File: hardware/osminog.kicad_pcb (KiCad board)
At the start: 2 copper layers, 16 parts, among them IC1 ATTINY2313-S, P1 USB_OTG, P2 CONN_01X02, P3 CONN_02X03, P4 CONN_01X03, P5 CONN_01X03, Q1 BSS138, U1 CH340G, Y1 12

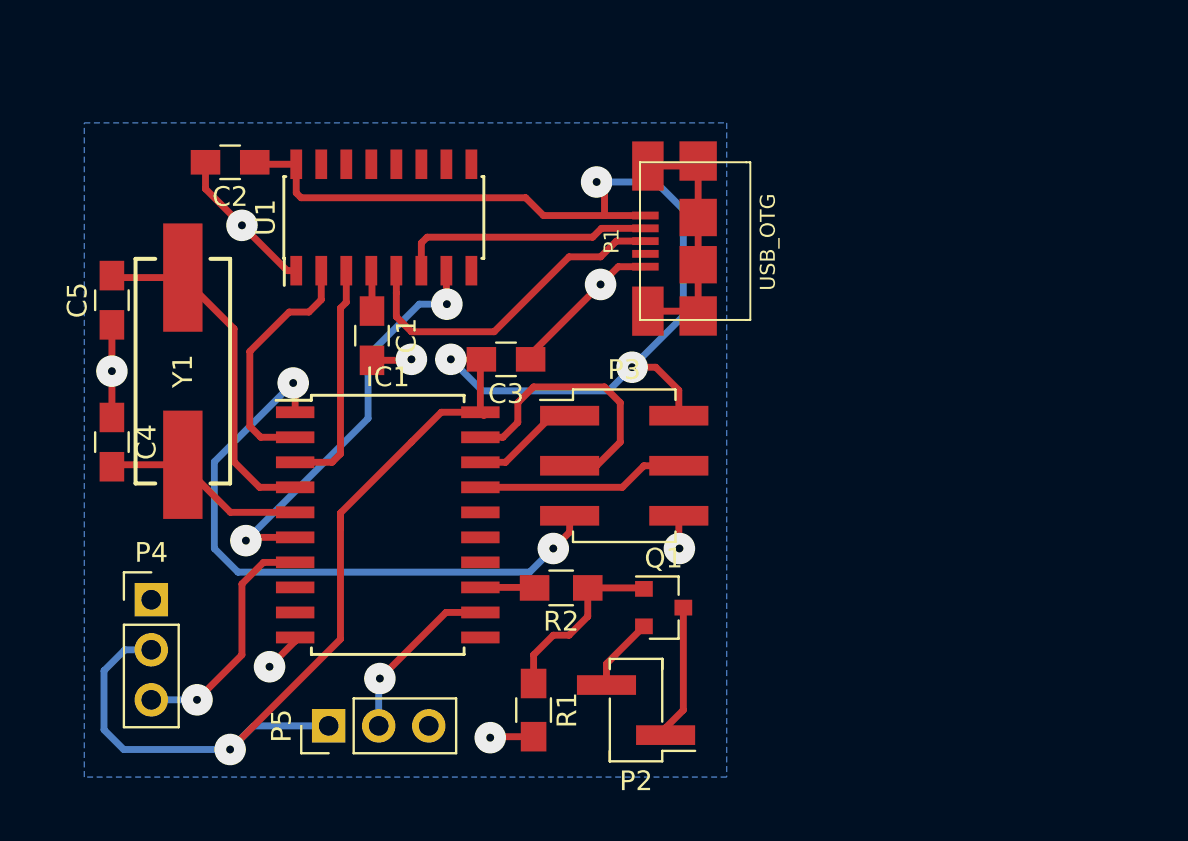
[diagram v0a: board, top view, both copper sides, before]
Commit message: Updating to use ATMEGA328pb...at less than 2USD, I might as well.
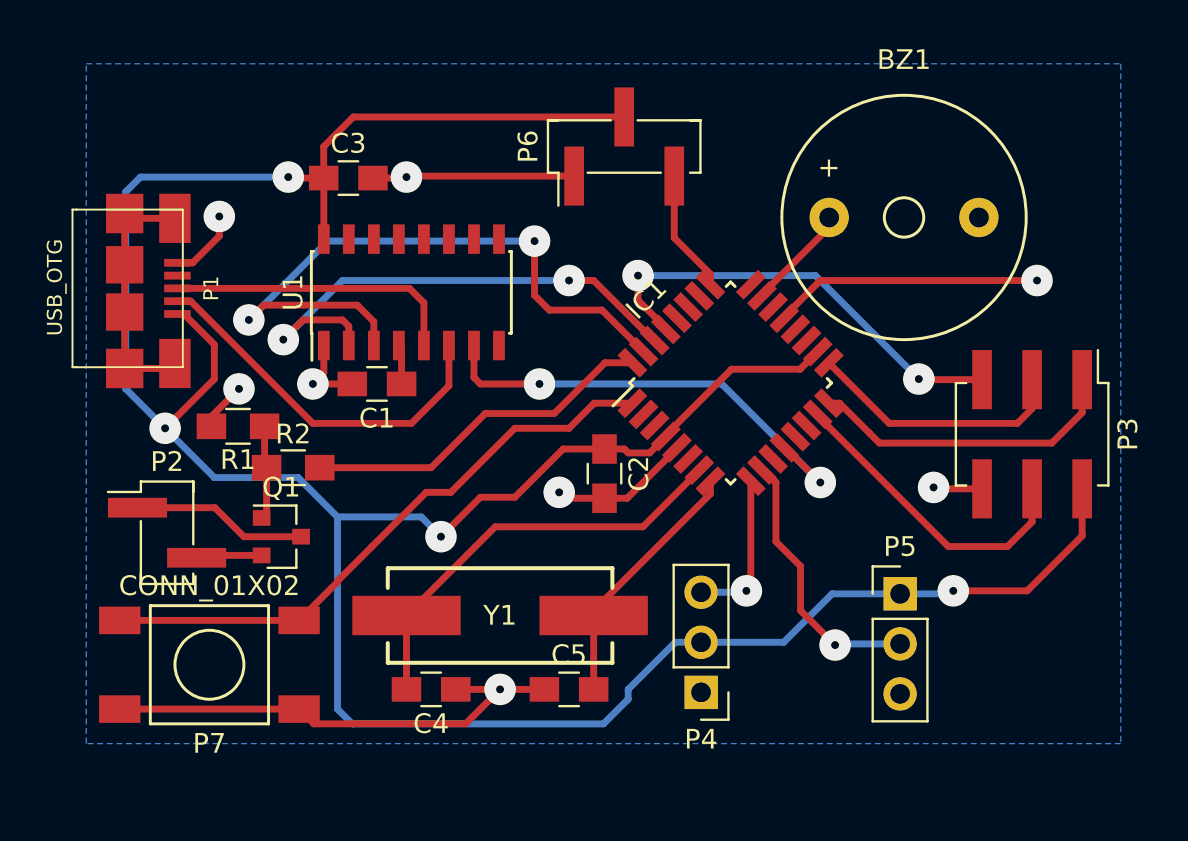
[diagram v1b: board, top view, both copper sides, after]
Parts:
- added BZ1: Buzzer, KiCad/Buzzers_Beepers.pretty:Buzzer_12x9.5RM7.6, F.Cu at (140.0, 46.8)
- added P6: CONN_01X03, KiCad/Pin_Headers.pretty:Pin_Header_Straight_1x03_Pitch2.54mm_SMD_Pin1Left, F.Cu at (125.8, 43.2)
- added P7: CONN_01X02, ojousima/Switches_buttons.pretty:SWITCH_FSM_JSM_off-mom, F.Cu at (104.8, 69.5)
- IC1: value ATTINY2313-S -> ATMEGA328PB-A; footprint KiCad/Housings_SOIC.pretty:SOIC-20W_7.5x12.8mm_Pitch1.27mm -> Housings_QFP:TQFP-32_7x7mm_Pitch0.8mm
- moved P1 32.1 mm to (99.0, 50.4), turned to 270 degrees
- moved C5 30.5 mm to (123.0, 70.8), turned to 0 degrees
- moved P5 29.8 mm to (139.8, 65.9), turned to 0 degrees
- moved P4 28.3 mm to (129.7, 70.9), turned to 180 degrees
- moved P2 25.4 mm to (102.6, 62.8), turned to 0 degrees
- moved C2 24.7 mm to (124.8, 59.8), turned to 270 degrees
- moved R1 20.8 mm to (106.2, 57.4), turned to 180 degrees
- moved P3 20.8 mm to (146.5, 57.8), turned to 270 degrees
- moved C4 20.5 mm to (116.0, 70.8), turned to 180 degrees
- moved Y1 20.3 mm to (119.5, 67.0), turned to 0 degrees
- moved Q1 19.7 mm to (108.4, 63.0)
- moved IC1 18.8 mm to (131.2, 55.2), turned to 45 degrees
- moved R2 14.9 mm to (109.0, 59.5), turned to 0 degrees
- moved C3 12.2 mm to (111.8, 44.8), turned to 0 degrees
- moved U1 4.05 mm to (115.0, 50.6)
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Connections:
- C3 pad 1: GND -> +5V
- C3 pad 2: +5V -> GND
- IC1 pad 1: RESET -> SWITCH
- IC1 pad 10: GND -> TEMP
- IC1 pad 12: TEMP -> CLKOUT
- IC1 pad 13: ENABLE_RELAY -> Net-(IC1-Pad13)
- IC1 pad 15: Net-(IC1-Pad15) -> MOSI
- IC1 pad 16: Net-(IC1-Pad16) -> MISO
- IC1 pad 17: MOSI -> SCK
- IC1 pad 18: MISO -> +5V
- IC1 pad 19: SCK -> Net-(IC1-Pad19)
- IC1 pad 20: +5V -> Net-(IC1-Pad20)
- IC1 pad 4: Net-(C5-Pad2) -> +5V
- IC1 pad 5: Net-(C4-Pad2) -> GND
- IC1 pad 6: CLKOUT -> Net-(IC1-Pad6)
- IC1 pad 7: XMIT -> Net-(C4-Pad2)
- IC1 pad 8: Net-(IC1-Pad8) -> Net-(C5-Pad2)
- IC1 pad 9: Net-(IC1-Pad9) -> XMIT
- U1 pad 2: Net-(IC1-Pad2) -> Net-(IC1-Pad30)
- U1 pad 3: Net-(IC1-Pad3) -> Net-(IC1-Pad31)
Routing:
- net +5V: track 99.0 -> 145.6 mm
- net GND: track 28.2 -> 68.8 mm, vias 7 -> 8
- net Net-(IC1-Pad31): track 0.00 -> 33.8 mm, vias 0 -> 2
- net SWITCH: track 0.00 -> 30.6 mm
- net Net-(IC1-Pad30): track 0.00 -> 26.2 mm, vias 0 -> 2
- net ENABLE_RELAY: track 2.76 -> 18.1 mm
- net Net-(IC1-Pad2): track 12.5 -> 0.00 mm
- net Net-(IC1-Pad3): track 11.9 -> 0.00 mm
- net Net-(C4-Pad2): track 10.3 -> 21.7 mm
- net MISO: track 5.51 -> 16.0 mm
- net RESET: track 32.6 -> 23.0 mm
- net LED: track 0.00 -> 6.27 mm
- net Net-(P1-Pad2): track 13.1 -> 19.2 mm
- net BUZZER: track 0.00 -> 5.39 mm
- net TEMP: track 8.91 -> 13.8 mm
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
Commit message: Adding latest version of osminog.
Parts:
- added C6: 0.1u, Capacitors_SMD:C_0805_HandSoldering, F.Cu at (116.0, 44.0)
- added R3: 10k, Resistors_SMD:R_0805_HandSoldering, F.Cu at (118.2, 44.0)
- R1: value R_Small -> 10k
- R2: value R_Small -> 470
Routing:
- net RESET: track 23.0 -> 36.7 mm, vias 2 -> 3
- net +5V: track 145.6 -> 154.2 mm
- net BUZZER: track 5.39 -> 8.81 mm, vias 0 -> 1
- net Net-(C6-Pad2): track 0.00 -> 3.33 mm
- net GND: track 68.8 -> 70.6 mm, vias 8 -> 9
